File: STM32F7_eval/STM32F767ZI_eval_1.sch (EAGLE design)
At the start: 102 parts, among them CN3 GROVE-4P-CONN-I2C-90D, CN4 GROVE-4P-CONN-I2C-90D, CN5 ARDUINO_COMPAT_IF, CN6 STLINKV21_SWD_IF, CN7 WFT0750CZ09-SMD_, CN9 UART_IF, Q1 PMF370XN_, SW1 SKRPACE010_, SW2 SKRPACE010_, U1 STM32F767ZI_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

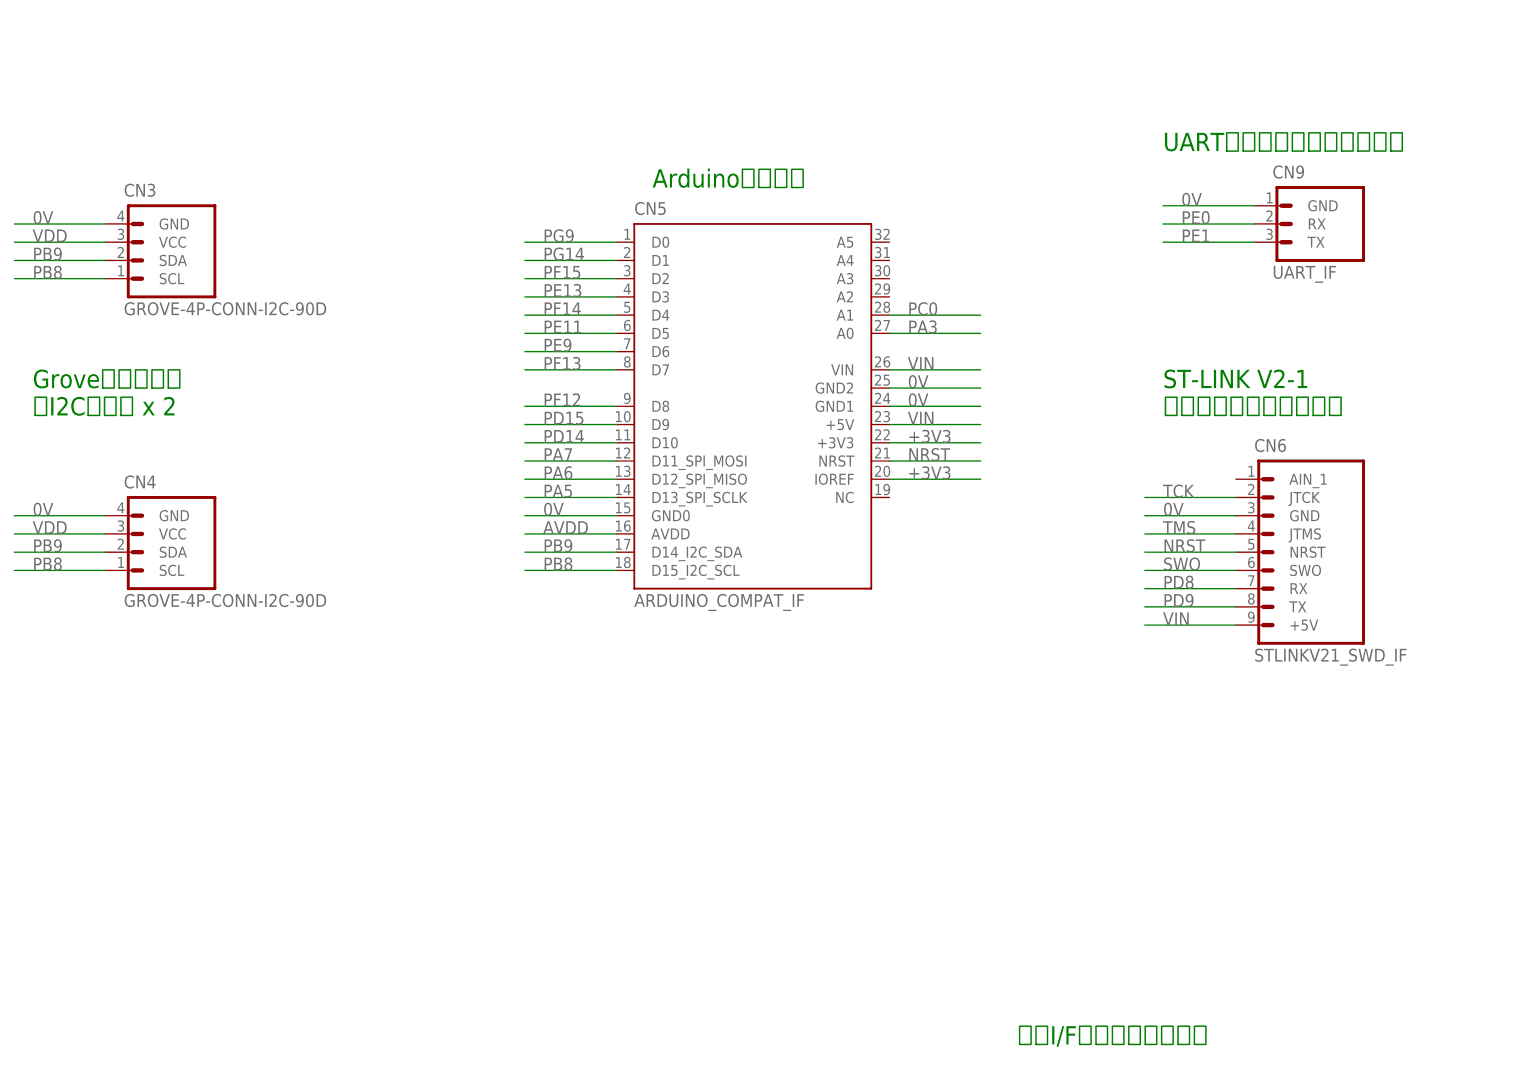
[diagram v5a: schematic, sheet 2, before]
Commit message: 回路図を修正
・ST-LINK V2-1インターフェースを他部品に変更
・外部フラッシュの電源をSTMの電源と切り離す
・Groveコネクターを基板の隅に移動
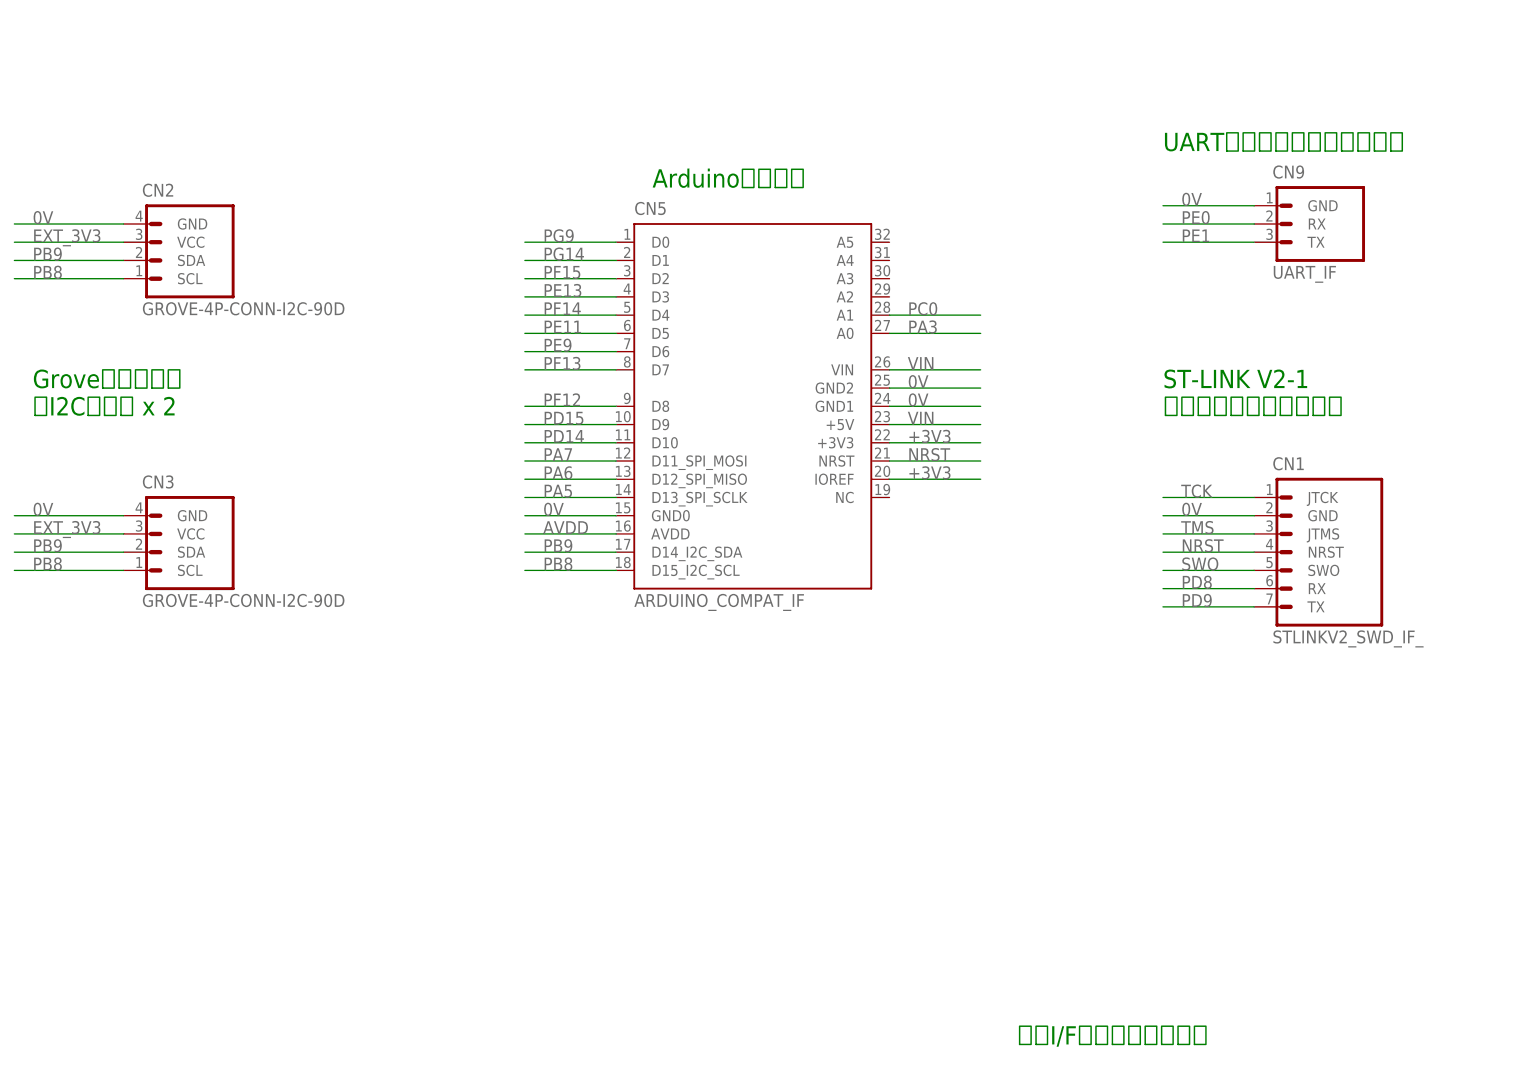
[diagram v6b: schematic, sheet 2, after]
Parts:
- removed CN4: GROVE-4P-CONN-I2C-90D, PartsForProto:GROVE-4P-CONN-I2C-90D
- removed CN6: STLINKV21_SWD_IF, PartsForProto:STLINKV21_SWD_IF
- added CN1: STLINKV2_SWD_IF_, Connectors:STLINKV2_SWD_IF_
- added CN2: GROVE-4P-CONN-I2C-90D, PartsForProto:GROVE-4P-CONN-I2C-90D
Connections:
- new net EXT_3V3: CN2.VCC, CN3.VCC, R25.1
- net +3V3: no longer R25.1
- net 0V: now also CN1.GND, CN2.GND; no longer CN4.GND, CN6.GND
- net NRST: now also CN1.NRST; no longer CN6.NRST
- net PB8: now also CN2.SCL; no longer CN4.SCL
- net PB9: now also CN2.SDA; no longer CN4.SDA
- net PD8: now also CN1.RX; no longer CN6.RX
- net PD9: now also CN1.TX; no longer CN6.TX
- net SWO: now also CN1.SWO; no longer CN6.SWO
- net TCK: now also CN1.JTCK; no longer CN6.JTCK
- net TMS: now also CN1.JTMS; no longer CN6.JTMS
- net VDD: no longer CN3.VCC, CN4.VCC
- net VIN: no longer CN6.+5V
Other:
- moved on the sheet: CN3
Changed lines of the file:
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@@
 <part name="R4" library="Parts" deviceset="RESISTOR" device="_0603_DEV" value="0"/>
 <part name="FRAME2" library="Generic" deviceset="A4L-LOC" device=""/>
-<part name="CN3" library="PartsForProto" deviceset="GROVE-4P-CONN-I2C" device="-90D"/>
-<part name="CN4" library="PartsForProto" deviceset="GROVE-4P-CONN-I2C" device="-90D"/>
 <part name="CN5" library="PartsForProto" deviceset="ARDUINO_COMPAT_IF" device=""/>
-<part name="CN6" library="PartsForProto" deviceset="STLINKV21_SWD_IF" device=""/>
 <part name="SW1" library="Parts" deviceset="SKRPACE010" device="_" value="SKRPACE010_"/>
 <part name="C17" library="Parts" deviceset="CAP" device="_0603_DEV" value="0.1uF"/>
@@
 <part name="C46" library="Parts" deviceset="CAP" device="_0603_DEV" value="0.1uF"/>
 <part name="R25" library="Parts" deviceset="RESISTOR" device="_0603_DEV" value="0"/>
-<part name="+3V4" library="Supply" deviceset="+3V3" device=""/>
 <part name="SUPPLY2" library="Supply" deviceset="+1V8" device=""/>
 <part name="FRAME5" library="Generic" deviceset="A4L-LOC" device=""/>
@@
 <part name="GND13" library="Supply" deviceset="0V" device=""/>
 <part name="R19" library="Parts" deviceset="RESISTOR" device="_0603_DEV" value="10"/>
+<part name="CN1" library="Connectors" deviceset="STLINKV2_SWD_IF" device="_"/>
+<part name="CN2" library="PartsForProto" deviceset="GROVE-4P-CONN-I2C" device="-90D"/>
+<part name="CN3" library="PartsForProto" deviceset="GROVE-4P-CONN-I2C" device="-90D"/>
 </parts>
 <sheets>
@@
 <instances>
 <instance part="FRAME2" gate="G$1" x="0" y="0"/>
-<instance part="CN3" gate="G$1" x="40.64" y="127"/>
-<instance part="CN4" gate="G$1" x="40.64" y="86.36"/>
 <instance part="CN5" gate="G$1" x="111.76" y="124.46"/>
-<instance part="CN6" gate="G$1" x="198.12" y="91.44"/>
 <instance part="CN9" gate="G$1" x="200.66" y="129.54"/>
+<instance part="CN1" gate="G$1" x="200.66" y="88.9"/>
+<instance part="CN2" gate="G$1" x="43.18" y="127"/>
+<instance part="CN3" gate="G$1" x="43.18" y="86.36"/>
 </instances>
 <busses>
@@
 <net name="0V" class="0">
 <segment>
-<pinref part="CN3" gate="G$1" pin="GND"/>
-<wire x1="40.64" y1="127" x2="27.94" y2="127" width="0.1524" layer="91"/>
+<wire x1="43.18" y1="127" x2="27.94" y2="127" width="0.1524" layer="91"/>
 <label x="30.48" y="127" size="1.778" layer="95"/>
+<pinref part="CN2" gate="G$1" pin="GND"/>
 </segment>
 <segment>
@@
 </segment>
 <segment>
-<pinref part="CN6" gate="G$1" pin="GND"/>
-<wire x1="198.12" y1="86.36" x2="185.42" y2="86.36" width="0.1524" layer="91"/>
-<label x="187.96" y="86.36" size="1.778" layer="95"/>
+<wire x1="200.66" y1="86.36" x2="187.96" y2="86.36" width="0.1524" layer="91"/>
+<label x="190.5" y="86.36" size="1.778" layer="95"/>
+<pinref part="CN1" gate="G$1" pin="GND"/>
 </segment>
 <segment>
@@
 </segment>
 <segment>
-<pinref part="CN4" gate="G$1" pin="GND"/>
-<wire x1="40.64" y1="86.36" x2="27.94" y2="86.36" width="0.1524" layer="91"/>
+<wire x1="43.18" y1="86.36" x2="27.94" y2="86.36" width="0.1524" layer="91"/>
 <label x="30.48" y="86.36" size="1.778" layer="95"/>
+<pinref part="CN3" gate="G$1" pin="GND"/>
 </segment>
 </net>
@@
 <net name="PB9" class="0">
 <segment>
-<pinref part="CN3" gate="G$1" pin="SDA"/>
-<wire x1="40.64" y1="121.92" x2="27.94" y2="121.92" width="0.1524" layer="91"/>
+<wire x1="43.18" y1="121.92" x2="27.94" y2="121.92" width="0.1524" layer="91"/>
 <label x="30.48" y="121.92" size="1.778" layer="95"/>
+<pinref part="CN2" gate="G$1" pin="SDA"/>
 </segment>
 <segment>
@@
 </segment>
 <segment>
-<pinref part="CN4" gate="G$1" pin="SDA"/>
-<wire x1="40.64" y1="81.28" x2="27.94" y2="81.28" width="0.1524" layer="91"/>
+<wire x1="43.18" y1="81.28" x2="27.94" y2="81.28" width="0.1524" layer="91"/>
 <label x="30.48" y="81.28" size="1.778" layer="95"/>
+<pinref part="CN3" gate="G$1" pin="SDA"/>
 </segment>
 </net>
 <net name="PB8" class="0">
 <segment>
-<pinref part="CN3" gate="G$1" pin="SCL"/>
-<wire x1="40.64" y1="119.38" x2="27.94" y2="119.38" width="0.1524" layer="91"/>
+<wire x1="43.18" y1="119.38" x2="27.94" y2="119.38" width="0.1524" layer="91"/>
 <label x="30.48" y="119.38" size="1.778" layer="95"/>
+<pinref part="CN2" gate="G$1" pin="SCL"/>
 </segment>
 <segment>
@@
 </segment>
 <segment>
-<pinref part="CN4" gate="G$1" pin="SCL"/>
-<wire x1="40.64" y1="78.74" x2="27.94" y2="78.74" width="0.1524" layer="91"/>
+<wire x1="43.18" y1="78.74" x2="27.94" y2="78.74" width="0.1524" layer="91"/>
 <label x="30.48" y="78.74" size="1.778" layer="95"/>
+<pinref part="CN3" gate="G$1" pin="SCL"/>
 </segment>
 </net>
@@
 <net name="TCK" class="0">
 <segment>
-<pinref part="CN6" gate="G$1" pin="JTCK"/>
-<wire x1="198.12" y1="88.9" x2="185.42" y2="88.9" width="0.1524" layer="91"/>
-<label x="187.96" y="88.9" size="1.778" layer="95"/>
+<wire x1="200.66" y1="88.9" x2="187.96" y2="88.9" width="0.1524" layer="91"/>
+<label x="190.5" y="88.9" size="1.778" layer="95"/>
+<pinref part="CN1" gate="G$1" pin="JTCK"/>
 </segment>
 </net>
 <net name="TMS" class="0">
 <segment>
-<pinref part="CN6" gate="G$1" pin="JTMS"/>
-<wire x1="198.12" y1="83.82" x2="185.42" y2="83.82" width="0.1524" layer="91"/>
-<label x="187.96" y="83.82" size="1.778" layer="95"/>
+<wire x1="200.66" y1="83.82" x2="187.96" y2="83.82" width="0.1524" layer="91"/>
+<label x="190.5" y="83.82" size="1.778" layer="95"/>
+<pinref part="CN1" gate="G$1" pin="JTMS"/>
 </segment>
 </net>
 <net name="NRST" class="0">
 <segment>
-<pinref part="CN6" gate="G$1" pin="NRST"/>
-<wire x1="198.12" y1="81.28" x2="185.42" y2="81.28" width="0.1524" layer="91"/>
-<label x="187.96" y="81.28" size="1.778" layer="95"/>
+<wire x1="200.66" y1="81.28" x2="187.96" y2="81.28" width="0.1524" layer="91"/>
+<label x="190.5" y="81.28" size="1.778" layer="95"/>
+<pinref part="CN1" gate="G$1" pin="NRST"/>
 </segment>
 <segment>
@@
 <net name="SWO" class="0">
 <segment>
-<pinref part="CN6" gate="G$1" pin="SWO"/>
-<wire x1="198.12" y1="78.74" x2="185.42" y2="78.74" width="0.1524" layer="91"/>
-<label x="187.96" y="78.74" size="1.778" layer="95"/>
+<wire x1="200.66" y1="78.74" x2="187.96" y2="78.74" width="0.1524" layer="91"/>
+<label x="190.5" y="78.74" size="1.778" layer="95"/>
+<pinref part="CN1" gate="G$1" pin="SWO"/>
 </segment>
 </net>
@@
 </segment>
 <segment>
-<pinref part="CN6" gate="G$1" pin="+5V"/>
-<wire x1="198.12" y1="71.12" x2="185.42" y2="71.12" width="0.1524" layer="91"/>
-<label x="187.96" y="71.12" size="1.778" layer="95"/>
-</segment>
-<segment>
 <pinref part="CN5" gate="G$1" pin="+5V"/>
 <wire x1="149.86" y1="99.06" x2="162.56" y2="99.06" width="0.1524" layer="91"/>
@@
 </segment>
 </net>
-<net name="VDD" class="0">
-<segment>
-<pinref part="CN3" gate="G$1" pin="VCC"/>
-<wire x1="40.64" y1="124.46" x2="27.94" y2="124.46" width="0.1524" layer="91"/>
-<label x="30.48" y="124.46" size="1.778" layer="95"/>
-</segment>
-<segment>
-<pinref part="CN4" gate="G$1" pin="VCC"/>
-<wire x1="40.64" y1="83.82" x2="27.94" y2="83.82" width="0.1524" layer="91"/>
-<label x="30.48" y="83.82" size="1.778" layer="95"/>
-</segment>
-</net>
 <net name="PD8" class="0">
 <segment>
-<pinref part="CN6" gate="G$1" pin="RX"/>
-<wire x1="198.12" y1="76.2" x2="185.42" y2="76.2" width="0.1524" layer="91"/>
-<label x="187.96" y="76.2" size="1.778" layer="95"/>
+<wire x1="200.66" y1="76.2" x2="187.96" y2="76.2" width="0.1524" layer="91"/>
+<label x="190.5" y="76.2" size="1.778" layer="95"/>
+<pinref part="CN1" gate="G$1" pin="RX"/>
 </segment>
 </net>
 <net name="PD9" class="0">
 <segment>
-<pinref part="CN6" gate="G$1" pin="TX"/>
-<wire x1="198.12" y1="73.66" x2="185.42" y2="73.66" width="0.1524" layer="91"/>
-<label x="187.96" y="73.66" size="1.778" layer="95"/>
+<wire x1="200.66" y1="73.66" x2="187.96" y2="73.66" width="0.1524" layer="91"/>
+<label x="190.5" y="73.66" size="1.778" layer="95"/>
+<pinref part="CN1" gate="G$1" pin="TX"/>
 </segment>
 </net>
@@
 <wire x1="200.66" y1="124.46" x2="187.96" y2="124.46" width="0.1524" layer="91"/>
 <label x="190.5" y="124.46" size="1.778" layer="95"/>
+</segment>
+</net>
+<net name="EXT_3V3" class="0">
+<segment>
+<pinref part="CN2" gate="G$1" pin="VCC"/>
+<wire x1="43.18" y1="124.46" x2="27.94" y2="124.46" width="0.1524" layer="91"/>
+<label x="30.48" y="124.46" size="1.778" layer="95"/>
+</segment>
+<segment>
+<pinref part="CN3" gate="G$1" pin="VCC"/>
+<wire x1="43.18" y1="83.82" x2="27.94" y2="83.82" width="0.1524" layer="91"/>
+<label x="30.48" y="83.82" size="1.778" layer="95"/>
 </segment>
 </net>
@@
 <instance part="C46" gate="G$1" x="208.28" y="73.66"/>
 <instance part="R25" gate="G$1" x="76.2" y="139.7"/>
-<instance part="+3V4" gate="G$1" x="71.12" y="152.4"/>
 <instance part="SUPPLY2" gate="G$1" x="134.62" y="93.98"/>
 <instance part="U5" gate="G$1" x="116.84" y="139.7"/>
@@
 </busses>
 <nets>
-<net name="+3V3" class="0">
-<segment>
-<pinref part="R25" gate="G$1" pin="1"/>
-<wire x1="76.2" y1="139.7" x2="71.12" y2="139.7" width="0.1524" layer="91"/>
-<pinref part="+3V4" gate="G$1" pin="+3V3"/>
-<wire x1="71.12" y1="139.7" x2="71.12" y2="149.86" width="0.1524" layer="91"/>
-</segment>
-</net>
 <net name="0V" class="0">
 <segment>
@@
 </segment>
 </net>
+<net name="EXT_3V3" class="0">
+<segment>
+<pinref part="R25" gate="G$1" pin="1"/>
+<wire x1="76.2" y1="139.7" x2="55.88" y2="139.7" width="0.1524" layer="91"/>
+<label x="58.42" y="139.7" size="1.778" layer="95"/>
+</segment>
+</net>

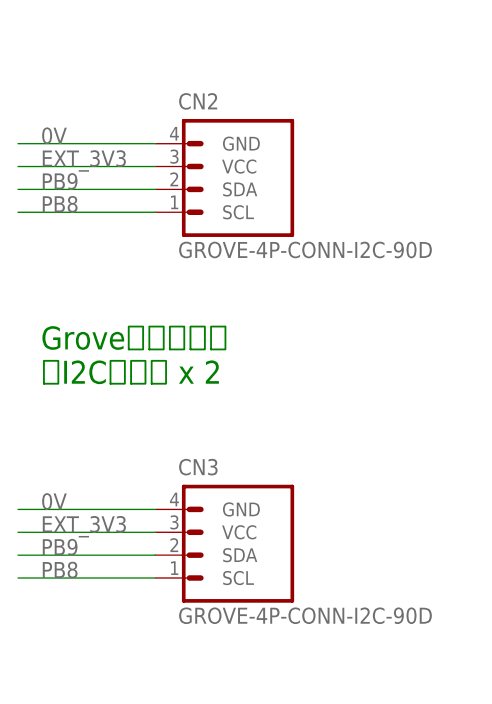
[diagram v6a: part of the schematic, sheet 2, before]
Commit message: 回路図を修正
・配線変更
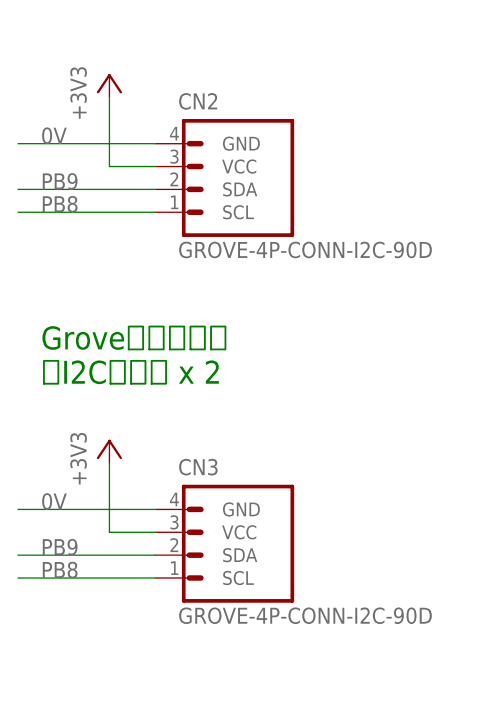
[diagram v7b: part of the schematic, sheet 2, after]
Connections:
- removed net EXT_3V3: CN2.VCC, CN3.VCC, R25.1
- net +3V3: now also CN2.VCC, CN3.VCC, R25.1
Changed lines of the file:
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@@
 <part name="CN2" library="PartsForProto" deviceset="GROVE-4P-CONN-I2C" device="-90D"/>
 <part name="CN3" library="PartsForProto" deviceset="GROVE-4P-CONN-I2C" device="-90D"/>
+<part name="+3V4" library="Supply" deviceset="+3V3" device=""/>
+<part name="+3V5" library="Supply" deviceset="+3V3" device=""/>
+<part name="+3V6" library="Supply" deviceset="+3V3" device=""/>
 </parts>
 <sheets>
@@
 <instance part="CN2" gate="G$1" x="43.18" y="127"/>
 <instance part="CN3" gate="G$1" x="43.18" y="86.36"/>
+<instance part="+3V5" gate="G$1" x="38.1" y="134.62"/>
+<instance part="+3V6" gate="G$1" x="38.1" y="93.98"/>
 </instances>
 <busses>
@@
 <label x="152.4" y="91.44" size="1.778" layer="95"/>
 </segment>
+<segment>
+<pinref part="CN3" gate="G$1" pin="VCC"/>
+<pinref part="+3V6" gate="G$1" pin="+3V3"/>
+<wire x1="43.18" y1="83.82" x2="38.1" y2="83.82" width="0.1524" layer="91"/>
+<wire x1="38.1" y1="83.82" x2="38.1" y2="91.44" width="0.1524" layer="91"/>
+</segment>
+<segment>
+<pinref part="CN2" gate="G$1" pin="VCC"/>
+<pinref part="+3V5" gate="G$1" pin="+3V3"/>
+<wire x1="43.18" y1="124.46" x2="38.1" y2="124.46" width="0.1524" layer="91"/>
+<wire x1="38.1" y1="124.46" x2="38.1" y2="132.08" width="0.1524" layer="91"/>
+</segment>
 </net>
 <net name="PB9" class="0">
@@
 <wire x1="200.66" y1="124.46" x2="187.96" y2="124.46" width="0.1524" layer="91"/>
 <label x="190.5" y="124.46" size="1.778" layer="95"/>
-</segment>
-</net>
-<net name="EXT_3V3" class="0">
-<segment>
-<pinref part="CN2" gate="G$1" pin="VCC"/>
-<wire x1="43.18" y1="124.46" x2="27.94" y2="124.46" width="0.1524" layer="91"/>
-<label x="30.48" y="124.46" size="1.778" layer="95"/>
-</segment>
-<segment>
-<pinref part="CN3" gate="G$1" pin="VCC"/>
-<wire x1="43.18" y1="83.82" x2="27.94" y2="83.82" width="0.1524" layer="91"/>
-<label x="30.48" y="83.82" size="1.778" layer="95"/>
 </segment>
 </net>
@@
 <instance part="GND13" gate="1" x="208.28" y="43.18"/>
 <instance part="R19" gate="G$1" x="93.98" y="27.94"/>
+<instance part="+3V4" gate="G$1" x="68.58" y="149.86"/>
 </instances>
 <busses>
@@
 </segment>
 </net>
-<net name="EXT_3V3" class="0">
+<net name="+3V3" class="0">
 <segment>
 <pinref part="R25" gate="G$1" pin="1"/>
-<wire x1="76.2" y1="139.7" x2="55.88" y2="139.7" width="0.1524" layer="91"/>
-<label x="58.42" y="139.7" size="1.778" layer="95"/>
-</segment>
-</net>
+<pinref part="+3V4" gate="G$1" pin="+3V3"/>
+<wire x1="76.2" y1="139.7" x2="68.58" y2="139.7" width="0.1524" layer="91"/>
+<wire x1="68.58" y1="139.7" x2="68.58" y2="147.32" width="0.1524" layer="91"/>
+</segment>
+</net>
